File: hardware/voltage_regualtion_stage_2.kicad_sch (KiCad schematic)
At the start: 29 parts, among them Q2 PMOS, Q3 PMOS, Q5 MUN5314DW1T1G, Q7 NMOS, U5 TSB712

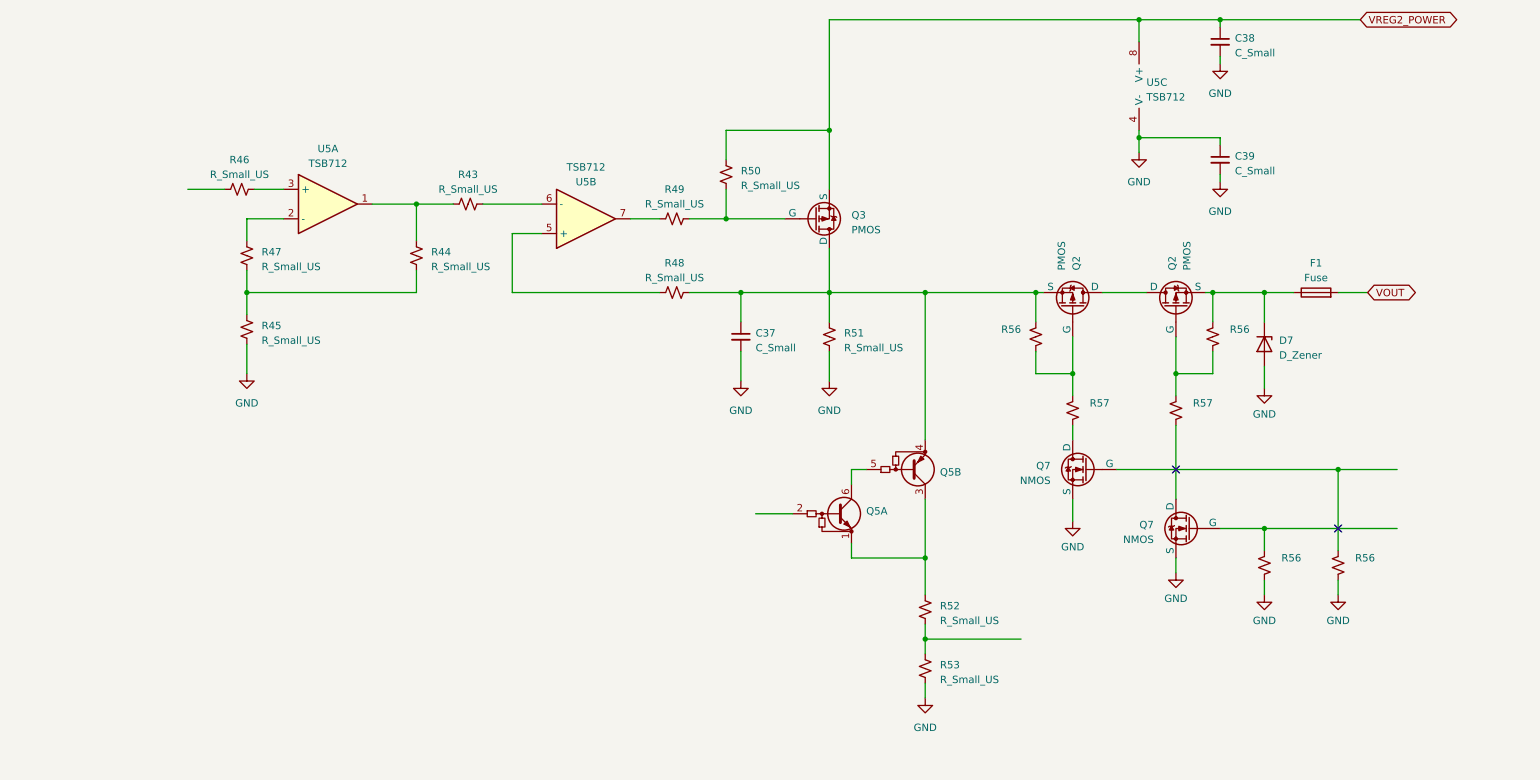
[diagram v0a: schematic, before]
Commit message: Component values chosen for bat. charge, bat. protect, USB input
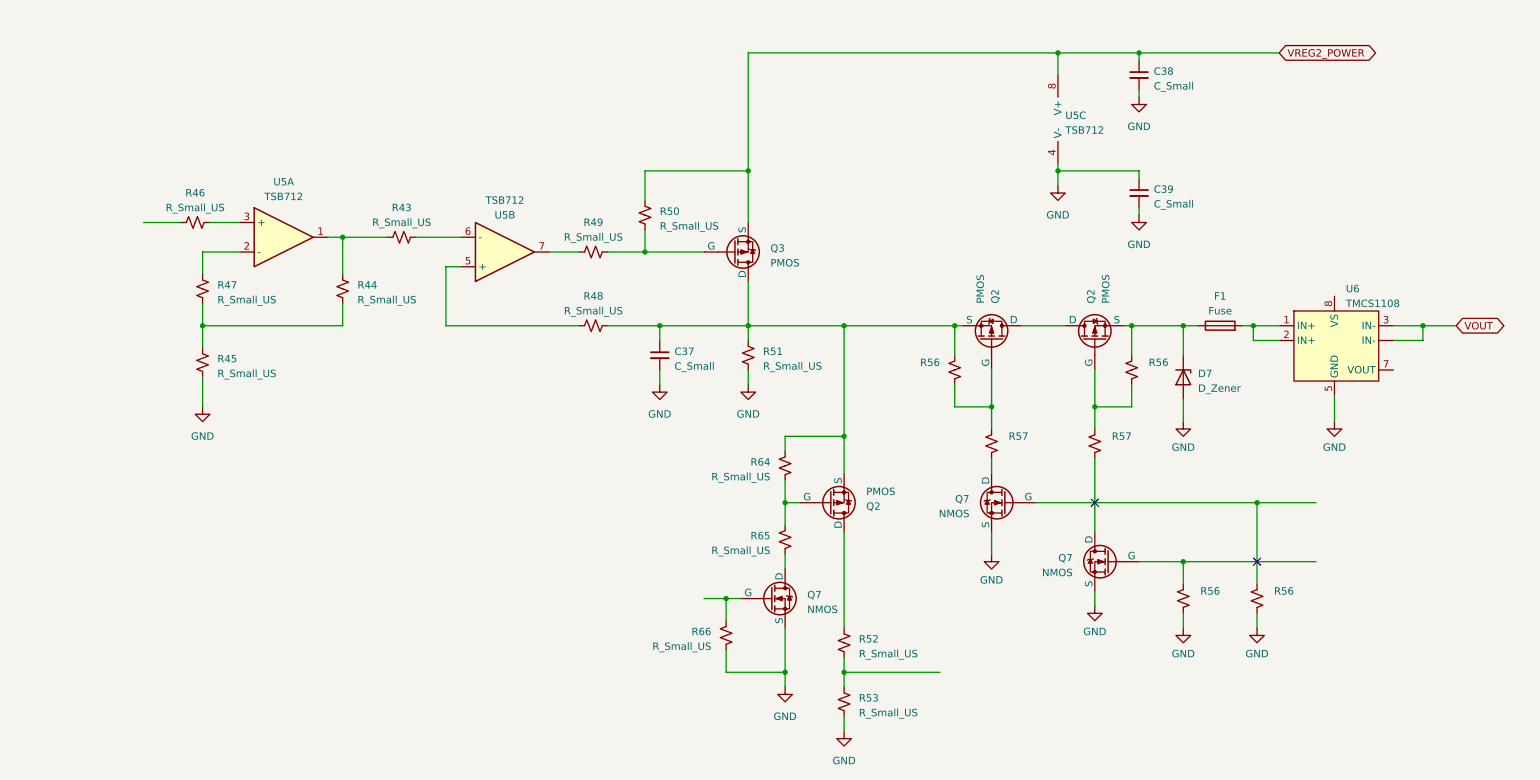
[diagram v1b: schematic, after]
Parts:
- removed Q5: MUN5314DW1T1G, Package_TO_SOT_SMD:SOT-363_SC-70-6, symbol Device:Q_Dual_NPN_PNP_BRT_E1B1C2E2B2C1
- added Q2: PMOS, symbol Simulation_SPICE:PMOS
- added Q7: NMOS, symbol Simulation_SPICE:NMOS
- added R64, R65, R66: R_Small_US, symbol Device:R_Small_US
- added U6: TMCS1108, Package_SO:SOIC-8_3.9x4.9mm_P1.27mm, symbol User_CurrentSense:TMCS1108
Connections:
- net GND: now also Q7.3 (S), R66.2, U6.5 (GND)
- net VOUT: now also U6. (IN-), U6.3 (IN-); no longer F1.2
- net at C37.1, Q2.3 (S), Q3.1 (D)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: now also Q2.3 (S), R64.1
- net at R52.1: now also Q2.1 (D)
- new net: F1.2, U6.1 (IN+), U6.2 (IN+)
- new net: Q2.2 (G), R64.2, R65.1
- new net: Q7.2 (G), R66.1
- new net: Q7.1 (D), R65.2
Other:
- moved on the sheet: C37, C38, C39, D7, F1, Q2, Q3, Q7, R43, R44, R45, R46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

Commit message: More simulation and work done on SEPIC stage. MOSFET changes to USB stage and charging stage.
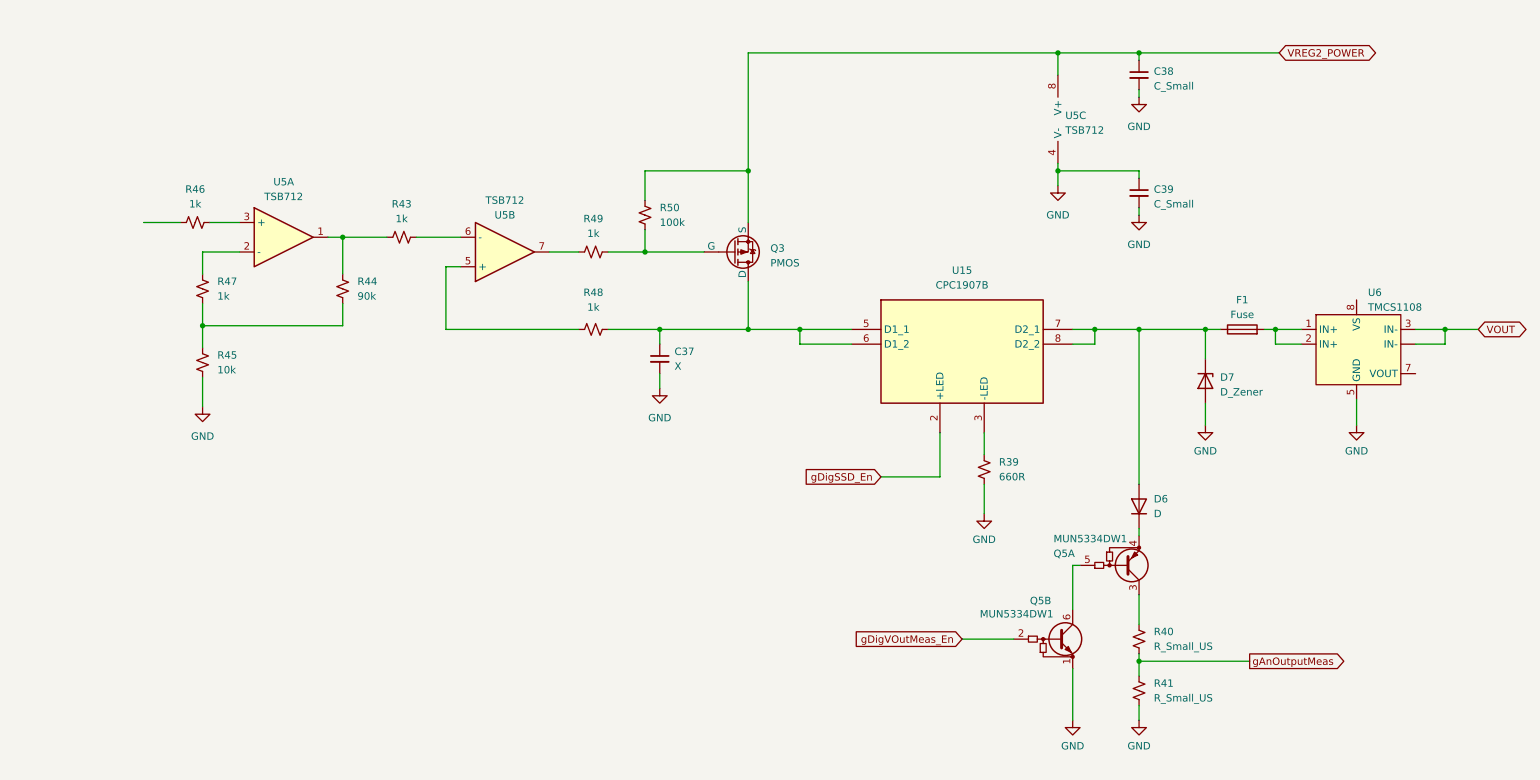
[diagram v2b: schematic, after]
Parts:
- removed Q2 (x3): PMOS, symbol Simulation_SPICE:PMOS
- removed Q7 (x3): NMOS, symbol Simulation_SPICE:NMOS
- removed R51, R52, R53, R64, R65, R66: R_Small_US, symbol Device:R_Small_US
- removed R56 (x4), R57 (x2): ~, symbol Device:R_Small_US
- added D6: D, symbol Device:D
- added Q5: MUN5334DW1, Package_TO_SOT_SMD:SOT-363_SC-70-6, symbol Transistor_BJT:MUN5334DW1
- added R39: 660R, symbol Device:R_Small_US
- added R40, R41: R_Small_US, symbol Device:R_Small_US
- added U15: CPC1907B, Daniel_Solid-State-Relay:CPC1907B, symbol Daniel_Solid-State-Relay:CPC1907B
- C37: value C_Small -> X
- R43, R46, R47, R48, R49: value R_Small_US -> 1k
- R44: value R_Small_US -> 90k
- R45: value R_Small_US -> 10k
- R50: value R_Small_US -> 100k
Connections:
- net GND: now also Q5.1 (E2), R39.2, R41.1
- net at C37.1, Q3.1 (D), R48.1: now also U15.5 (D1_1), U15.6 (D1_2)
- net at D7.1 (K), F1.1: now also D6.2 (A), U15.7 (D2_1), U15.8 (D2_2)
- new net: Q5.5 (B1), Q5.6 (C2)
- new net: R39.1, U15.3 (-LED)
- new net: U15.1 (N/C_1), U15.4 (N/C_2)
- new net: Q5.3 (C1), R40.2
- new net: D6.1 (K), Q5.4 (E1)
- new net gAnOutputMeas: R40.1, R41.2
- new net gDigSSD_En: U15.2 (+LED)
- new net gDigVOutMeas_En: Q5.2 (B2)
- no-connect marks 2 -> 0
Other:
- moved on the sheet: C37, D7, F1, R48, U6

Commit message: Saving prior to changing project structure
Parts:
- removed Q3: PMOS, symbol Simulation_SPICE:PMOS
- removed R39: 660R, symbol Device:R_Small_US
- removed U15: CPC1907B, Daniel_Solid-State-Relay:CPC1907B, symbol Daniel_Solid-State-Relay:CPC1907B
- added C25, C36: 330u, symbol Device:C_Polarized_US
- added C45: 1u, symbol Device:C_Small
- added C46, C47: 0.1u, symbol Device:C_Small
- added D13: FERD20H100SB, symbol Daniel_Diode:D_AKA
- added Q11: STL45P3LLH6, Daniel_xMOS:PowerFLAT 5x6, symbol Daniel_PMOS:Q_PMOS_DGS
- C37: value X -> 1u
- C38, C39: value C_Small -> 0.1u
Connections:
- net GND: now also C25.2, C36.2, C45.2, C46.2, C47.2, D13.1 (A), D13.3 (A)
- net VREG2_POWER: now also Q11.1 (S), Q11.2 (D), Q11.3 (D)
- net at D6.2 (A), D7.1 (K), F1.1: now also C37.1, R48.1, C25.1, C36.1, C45.1, C46.1, C47.1, D13.2 (K), Q11.5 (D), Q11.6 (D), Q11.7 (G), Q11.8 (D)
- net at R49.2, R50.1: now also Q11.7 (G)
- net gAnOutputVoltageSetpoint: now reaches R46.1
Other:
- moved on the sheet: C37, C38, C39, D6, D7, F1, Q5A, Q5B, R40, R41, R43, R44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
